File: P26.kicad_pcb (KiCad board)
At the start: 2 copper layers, 41.7 x 21.3 mm, 42 parts, among them IC1 DRV8231ADSGR, J1 Conn_01x08, J2 Conn_01x16, J3 Conn_01x02, J4 Conn_01x02, Q1 BC847BDW1, Q2 BC857BDW1, U1 TPS22810DRVR, U2 MIC5205-3.3YM5

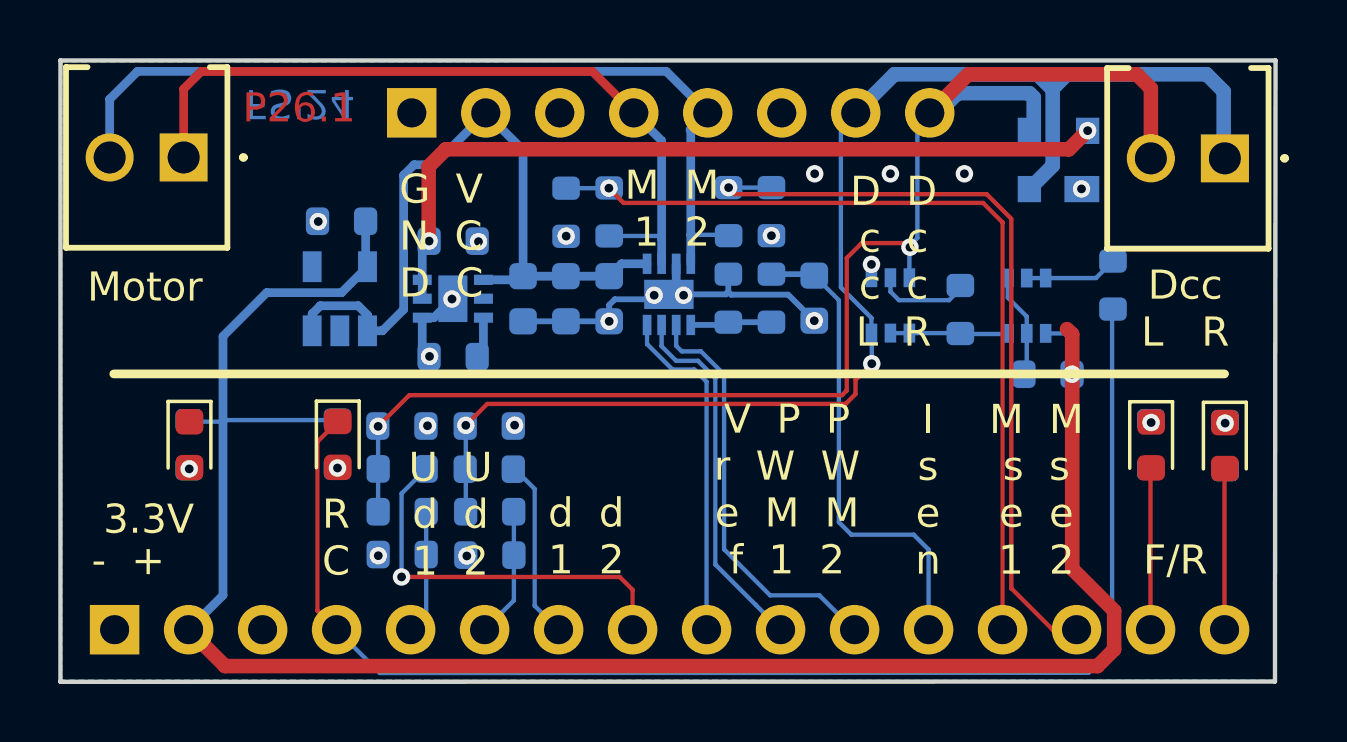
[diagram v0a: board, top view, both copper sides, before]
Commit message: mod: optimized for PCB assembly
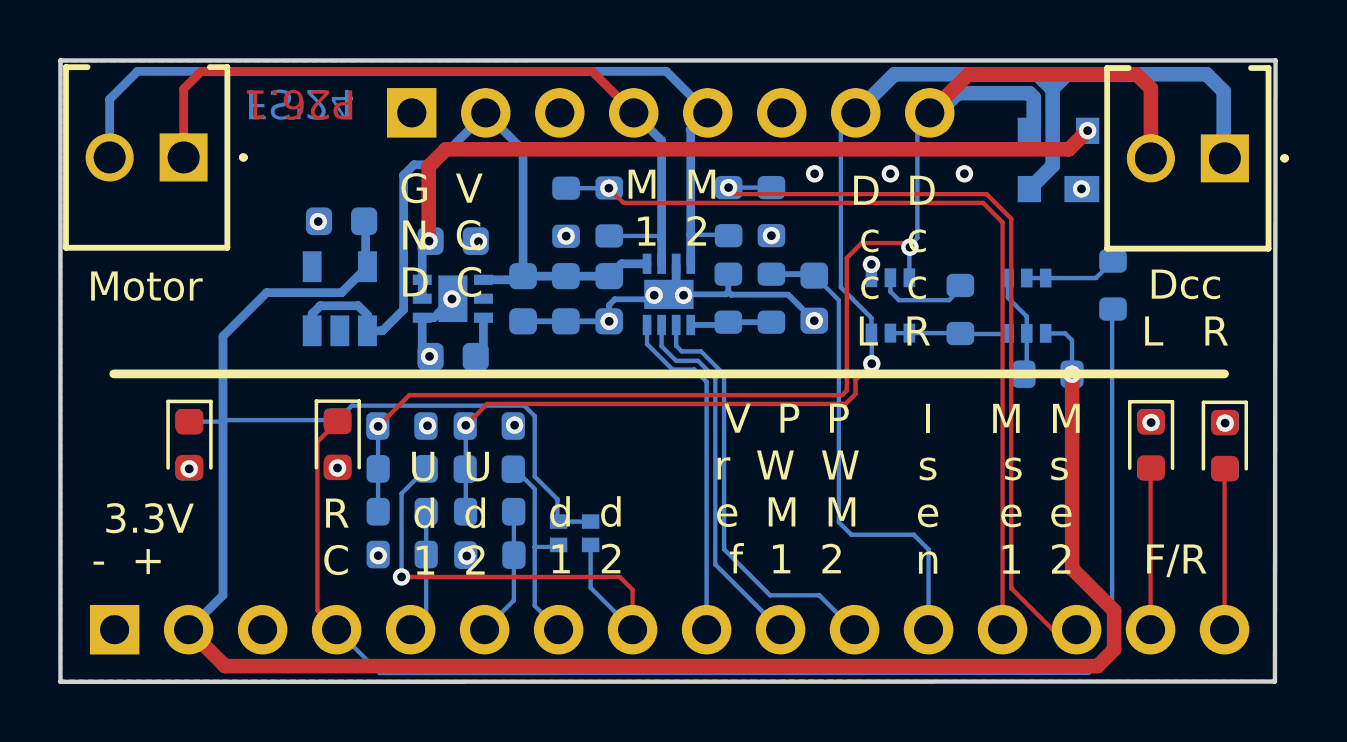
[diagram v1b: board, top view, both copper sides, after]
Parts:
- added D6: D_Schottky, RTB:SM5819L2TP, B.Cu at (90.6, -43.0)
- added D7: D_Schottky, RTB:SM5819L2TP, B.Cu at (89.5, -43.0)
- C1, C7: value 10u/25V -> 10u
- C2: value 100nF -> 100n; footprint Resistor_SMD:R_0603_1608Metric -> Capacitor_SMD:C_0603_1608Metric
- C3: value 22u/6V -> 22u; footprint Resistor_SMD:R_0603_1608Metric -> Capacitor_SMD:C_0603_1608Metric
- C4: value 100n/35V -> 100n
- C5: value 1u/35V -> 1u; footprint Resistor_SMD:R_0603_1608Metric -> Capacitor_SMD:C_0603_1608Metric
- D2, D3: value LED -> LED (wht)
- D4: value LED -> LED (blue)
- D5: value LED -> LED (green)
- J1: value Conn_01x08 -> High Voltage I/O
- J2: value Conn_01x16 -> Low voltage I/O
- J3: value Conn_01x02 -> DC motor output
- J4: value Conn_01x02 -> DCC input
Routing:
- net +3V3: track 69.7 -> 80.2 mm
- net Net-(D6-Pad2): track 13.5 -> 17.0 mm
- net Net-(D7-Pad2): track 6.18 -> 7.03 mm

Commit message: mod: conversion to KiCad 9
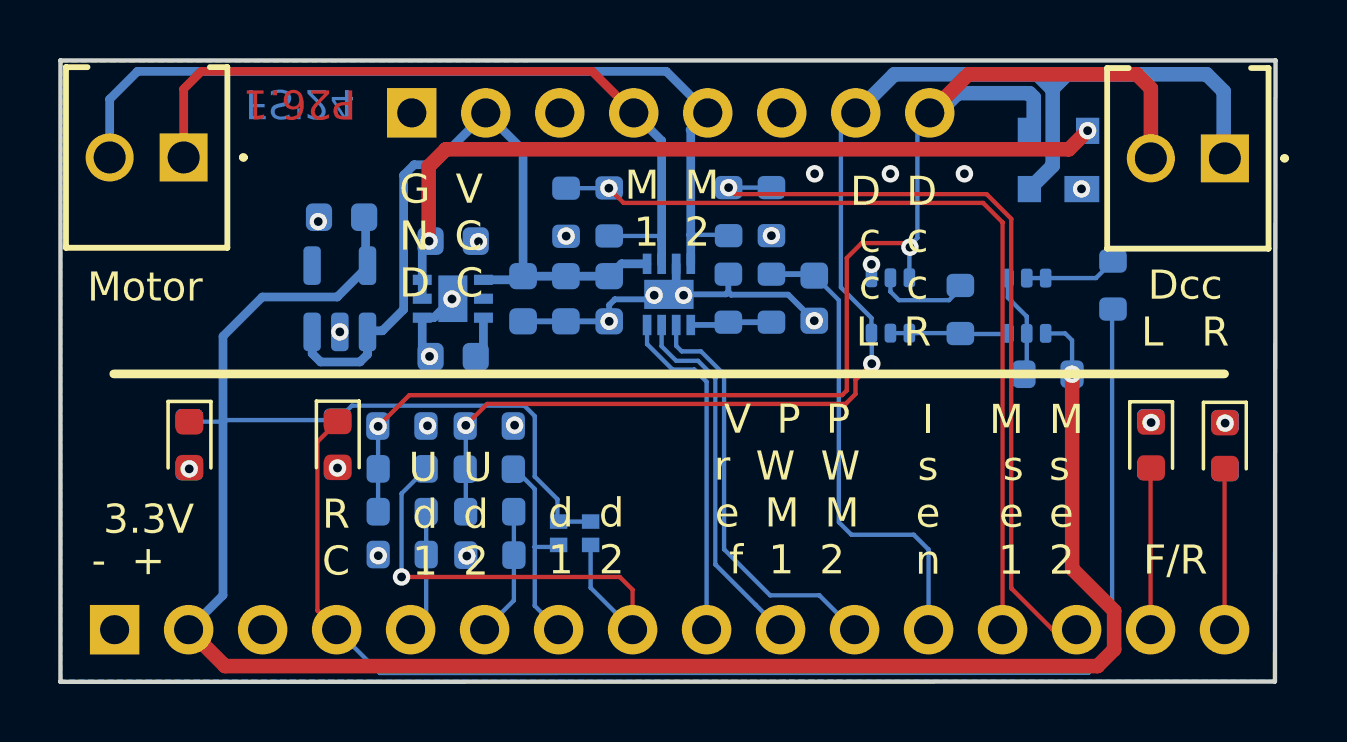
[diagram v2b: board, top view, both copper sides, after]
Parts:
- moved C3 0.14 mm to (82.0, -53.8)
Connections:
- J1 pad 3: (no net) -> unconnected-(J1-Pin_3-Pad3)
- J1 pad 6: (no net) -> unconnected-(J1-Pin_6-Pad6)
- J2 pad 3: (no net) -> unconnected-(J2-Pin_3-Pad3)
- U1 pad 2: (no net) -> unconnected-(U1-QOD-Pad2)
- U2 pad 4: (no net) -> unconnected-(U2-BP-Pad4)
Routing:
- net GND: vias 19 -> 20
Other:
- net class Default removed
- net class Power removed
